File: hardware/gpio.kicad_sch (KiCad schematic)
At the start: 10 parts, among them U26 W65C22SxP, U27 74HC541, U28 74HC541

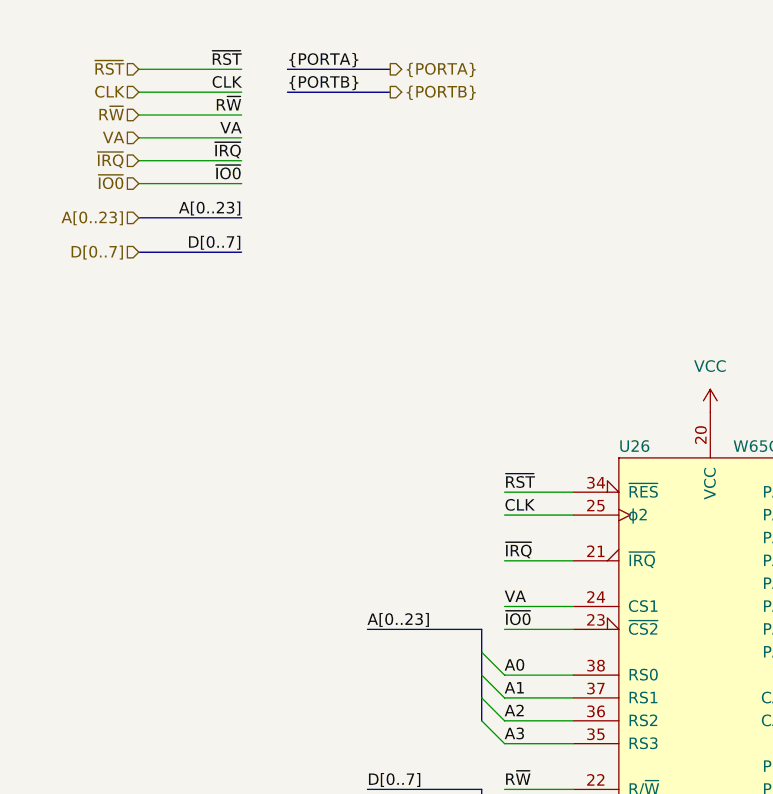
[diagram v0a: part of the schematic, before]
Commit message: Add 65C51
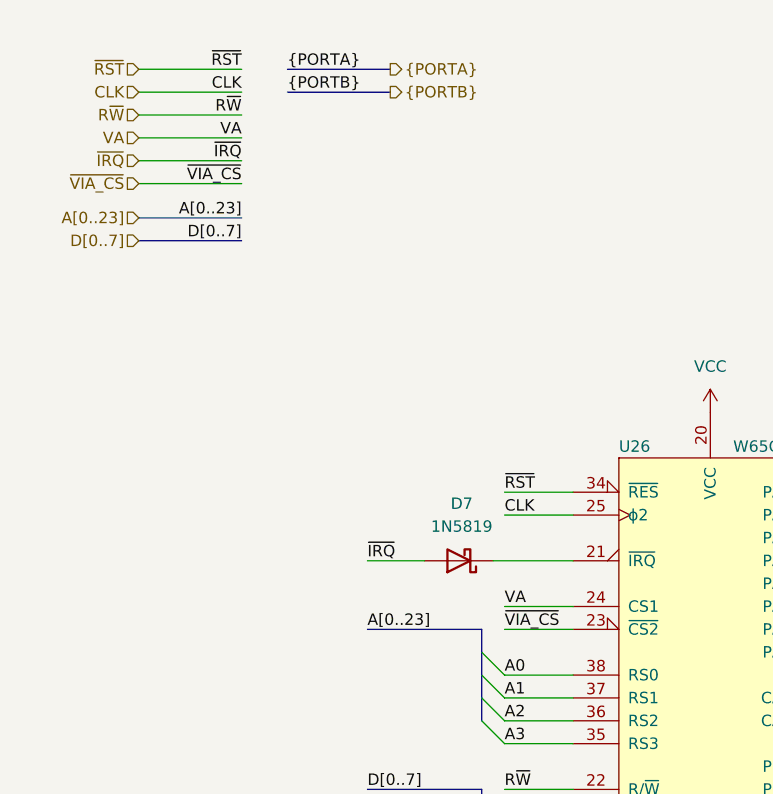
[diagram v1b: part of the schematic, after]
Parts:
- added D7: 1N5819, Diode_THT:D_DO-41_SOD81_P10.16mm_Horizontal, symbol Diode:1N5819
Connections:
- net ~{IRQ}: now also D7.2 (A); no longer U26.21 (~{IRQ})
- net ~{IO0} renamed ~{VIA_CS}
- new net: D7.1 (K), U26.21 (~{IRQ})
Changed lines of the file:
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@@
   (title_block
     (title "GPIO module")
-    (date "2022-09-03")
-    (rev "A.28")
+    (date "2022-09-26")
+    (rev "A.30")
     (comment 2 "https://github.com/adrienkohlbecker/65C816")
     (comment 3 "Licensed under CERN-OHL-W v2")
@@
     (stroke (width 0) (type default) (color 0 0 0 0))
   )
-  (wire (pts (xy 68.58 77.47) (xy 76.2 77.47))
+  (wire (pts (xy 53.34 77.47) (xy 59.69 77.47))
     (stroke (width 0) (type default) (color 0 0 0 0))
   )
@@
     (stroke (width 0) (type default) (color 0 0 0 0))
   )
+  (wire (pts (xy 67.31 77.47) (xy 76.2 77.47))
+    (stroke (width 0) (type default) (color 0 0 0 0))
+  )
   (wire (pts (xy 176.53 29.21) (xy 168.91 29.21))
     (stroke (width 0) (type default) (color 0 0 0 0))
@@
     (stroke (width 0) (type default) (color 0 0 0 0))
   )
-  (bus (pts (xy 27.94 43.18) (xy 39.37 43.18))
+  (bus (pts (xy 27.94 41.91) (xy 39.37 41.91))
     (stroke (width 0) (type default) (color 0 0 0 0))
   )
@@
     (effects (font (size 1.27 1.27)) (justify left bottom))
   )
-  (label "D[0..7]" (at 39.37 43.18 180)
+  (label "D[0..7]" (at 39.37 41.91 180)
     (effects (font (size 1.27 1.27)) (justify right bottom))
   )
@@
     (effects (font (size 1.27 1.27)) (justify left bottom))
   )
-  (label "~{IO0}" (at 39.37 35.56 180)
-    (effects (font (size 1.27 1.27)) (justify right bottom))
-  )
-  (label "~{IO0}" (at 68.58 85.09 0)
+  (label "~{VIA_CS}" (at 39.37 35.56 180)
+    (effects (font (size 1.27 1.27)) (justify right bottom))
+  )
+  (label "~{VIA_CS}" (at 68.58 85.09 0)
     (effects (font (size 1.27 1.27)) (justify left bottom))
   )
@@
     (effects (font (size 1.27 1.27)) (justify right bottom))
   )
-  (label "~{IRQ}" (at 68.58 77.47 0)
+  (label "~{IRQ}" (at 53.34 77.47 0)
     (effects (font (size 1.27 1.27)) (justify left bottom))
   )
@@
     (effects (font (size 1.27 1.27)) (justify right))
   )
-  (hierarchical_label "D[0..7]" (shape input) (at 27.94 43.18 180)
+  (hierarchical_label "D[0..7]" (shape input) (at 27.94 41.91 180)
     (effects (font (size 1.27 1.27)) (justify right))
   )
-  (hierarchical_label "~{IO0}" (shape input) (at 27.94 35.56 180)
+  (hierarchical_label "~{VIA_CS}" (shape input) (at 27.94 35.56 180)
     (effects (font (size 1.27 1.27)) (justify right))
   )
@@
     (pin "1")
   )
+  (symbol (lib_id "Diode:1N5819") (at 63.5 77.47 180) (unit 1)
+    (in_bom yes) (on_board yes) (fields_autoplaced)
+    (property "Reference" "D7" (id 0) (at 63.8175 71.12 0))
+    (property "Value" "1N5819" (id 1) (at 63.8175 73.66 0))
+    (property "Footprint" "Diode_THT:D_DO-41_SOD81_P10.16mm_Horizontal" (id 2) (at 63.5 73.025 0)
+      (effects (font (size 1.27 1.27)) hide)
+    )
+    (property "Datasheet" "http://www.vishay.com/docs/88525/1n5817.pdf" (id 3) (at 63.5 77.47 0)
+      (effects (font (size 1.27 1.27)) hide)
+    )
+    (pin "1")
+    (pin "2")
+  )
   (symbol (lib_id "power:GND") (at 91.44 134.62 0) (unit 1)

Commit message: Update schematic
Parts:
- added BAR10: Green, symbol 65C816:LED-Array-8
- added C44: 100n, symbol Device:C_Small
- added RN9: 3.3k, Resistor_THT:R_Array_SIP9, symbol Device:R_Network08
- added U33: 74HC541, symbol 74xx:74LS541
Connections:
- net CA1: now also U33.7 (A5)
- net CA2: now also U33.6 (A4)
- net CB1: now also U33.9 (A7)
- net CB2: now also U33.8 (A6)
- net GND: now also C44.2, RN9.1 (common), U33.1 (G1), U33.10 (GND), U33.19 (G2), U33.2 (A0), U33.3 (A1), U33.4 (A2), U33.5 (A3)
- net VCC: now also C44.1, U33.20 (VCC)
- new net: BAR10.9 (K), RN9.2 (R1)
- new net: BAR10.10 (K), RN9.3 (R2)
- new net: BAR10.11 (K), RN9.4 (R3)
- new net: BAR10.12 (K), RN9.5 (R4)
- new net: BAR10.13 (K), RN9.6 (R5)
- new net: BAR10.14 (K), RN9.7 (R6)
- new net: BAR10.15 (K), RN9.8 (R7)
- new net: BAR10.16 (K), RN9.9 (R8)
- new net: BAR10.1 (A), U33.18 (Y0)
- new net: BAR10.2 (A), U33.17 (Y1)
- new net: BAR10.3 (A), U33.16 (Y2)
- new net: BAR10.4 (A), U33.15 (Y3)
- new net: BAR10.5 (A), U33.14 (Y4)
- new net: BAR10.6 (A), U33.13 (Y5)
- new net: BAR10.7 (A), U33.12 (Y6)
- new net: BAR10.8 (A), U33.11 (Y7)
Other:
- moved on the sheet: BAR6, BAR7, C34, C35, C36, D7, RN5, RN6, U26, U27, U28

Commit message: Update for Episode 32
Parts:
- removed BAR10: Green, symbol 65C816:LED-Array-8
- removed RN9: 3.3k, Resistor_THT:R_Array_SIP9, symbol Device:R_Network08
- added BAR10: LED-Array-8-GYR, symbol 65C816:LED-Array-8-GYR
- added R30: 1.5k, symbol Device:R_Small
- added R31, R32: 1k, symbol Device:R_Small
- added R33, R48, R49, R50, R51: 6.8k, symbol Device:R_Small
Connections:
- net GND: now also R30.2, R31.2, R32.2, R33.2, R48.2, R49.2, R50.2, R51.2; no longer U33.2 (A0), U33.3 (A1), U33.4 (A2), U33.5 (A3)
- net at U33.18 (Y0): now also BAR10.8 (A)
- net at U33.17 (Y1): now also BAR10.7 (A)
- net at U33.16 (Y2): now also BAR10.6 (A)
- net at U33.15 (Y3): now also BAR10.5 (A)
- net at U33.14 (Y4): now also BAR10.4 (A)
- net at U33.13 (Y5): now also BAR10.3 (A)
- net at U33.12 (Y6): now also BAR10.2 (A)
- net at U33.11 (Y7): now also BAR10.1 (A)
- new net: BAR10.10 (K), R31.1
- new net: BAR10.11 (K), R32.1
- new net: BAR10.12 (K), R33.1
- new net: BAR10.13 (K), R48.1
- new net: BAR10.14 (K), R49.1
- new net: BAR10.15 (K), R50.1
- new net: BAR10.16 (K), R51.1
- new net: BAR10.9 (K), R30.1
- new net LED_I2C: U33.5 (A3)
- new net LED_RX: U33.3 (A1)
- new net LED_TX: U33.4 (A2)
- new net ~{USBCFG}: U33.2 (A0)

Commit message: Rename
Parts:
- BAR10: symbol 65C816:LED-Array-8-GYR -> BB816:LED-Array-8-GYR
- BAR6, BAR7: symbol 65C816:LED-Array-8 -> BB816:LED-Array-8
- U26: symbol 65C816:W65C22SxP -> BB816:W65C22SxP
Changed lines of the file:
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@@
   (title_block
     (title "GPIO module")
-    (date "2023-05-14")
+    (date "2023-05-23")
     (rev "A.32")
-    (comment 2 "https://github.com/adrienkohlbecker/65C816")
+    (comment 2 "https://github.com/adrienkohlbecker/BB816")
     (comment 3 "Licensed under CERN-OHL-W v2")
-    (comment 4 "Copyright © 2022 Adrien Kohlbecker")
+    (comment 4 "Copyright © 2022-2023 Adrien Kohlbecker")
   )
   (bus_alias "PORTA" (members "PA0" "PA1" "PA2" "PA3" "PA4" "PA5" "PA6" "PA7" "CA1" "CA2"))
@@
     (pin "9")
   )
-  (symbol (lib_id "65C816:LED-Array-8-GYR") (at 190.5 147.32 0) (mirror x) (unit 1)
+  (symbol (lib_id "BB816:LED-Array-8-GYR") (at 190.5 147.32 0) (mirror x) (unit 1)
     (in_bom yes) (on_board yes) (fields_autoplaced)
     (property "Reference" "BAR10" (id 0) (at 191.135 128.27 0))
@@
     (pin "1")
   )
-  (symbol (lib_id "65C816:W65C22SxP") (at 68.58 95.25 0) (unit 1)
+  (symbol (lib_id "BB816:W65C22SxP") (at 68.58 95.25 0) (unit 1)
     (in_bom yes) (on_board yes)
     (property "Reference" "U26" (id 0) (at 58.42 62.23 0)
@@
     (pin "1")
   )
-  (symbol (lib_id "65C816:LED-Array-8") (at 190.5 38.1 0) (unit 1)
+  (symbol (lib_id "BB816:LED-Array-8") (at 190.5 38.1 0) (unit 1)
     (in_bom yes) (on_board yes)
     (property "Reference" "BAR6" (id 0) (at 190.5 23.241 0))
@@
     (pin "1")
   )
-  (symbol (lib_id "65C816:LED-Array-8") (at 190.5 91.44 0) (unit 1)
+  (symbol (lib_id "BB816:LED-Array-8") (at 190.5 91.44 0) (unit 1)
     (in_bom yes) (on_board yes)
     (property "Reference" "BAR7" (id 0) (at 190.5 76.581 0))
